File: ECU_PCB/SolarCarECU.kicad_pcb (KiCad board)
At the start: 4 copper layers, 160 x 105.4 mm, 231 parts, among them J2 Screw_Terminal_01x08, J3 Screw_Terminal_01x08, J4 Screw_Terminal_01x08, J5 Screw_Terminal_01x08, J6 Screw_Terminal_01x08, J7 Screw_Terminal_01x08, J8 Screw_Terminal_01x08, Q1 QM6015D, Q2 QM6015D, Q3 QM6015D, Q4 QM6015D, Q5 QM6015D, Q6 QM6015D, Q7 QM6015D, U1 Teensy3.6, U10 LM324A, U11 MCP1403, U2 MCP1403, U3 MCP1403, U4 L7805, U5 MCP2562-E-P, U6 MCP2562-E-P, U7 4504, U8 4504, U9 4504

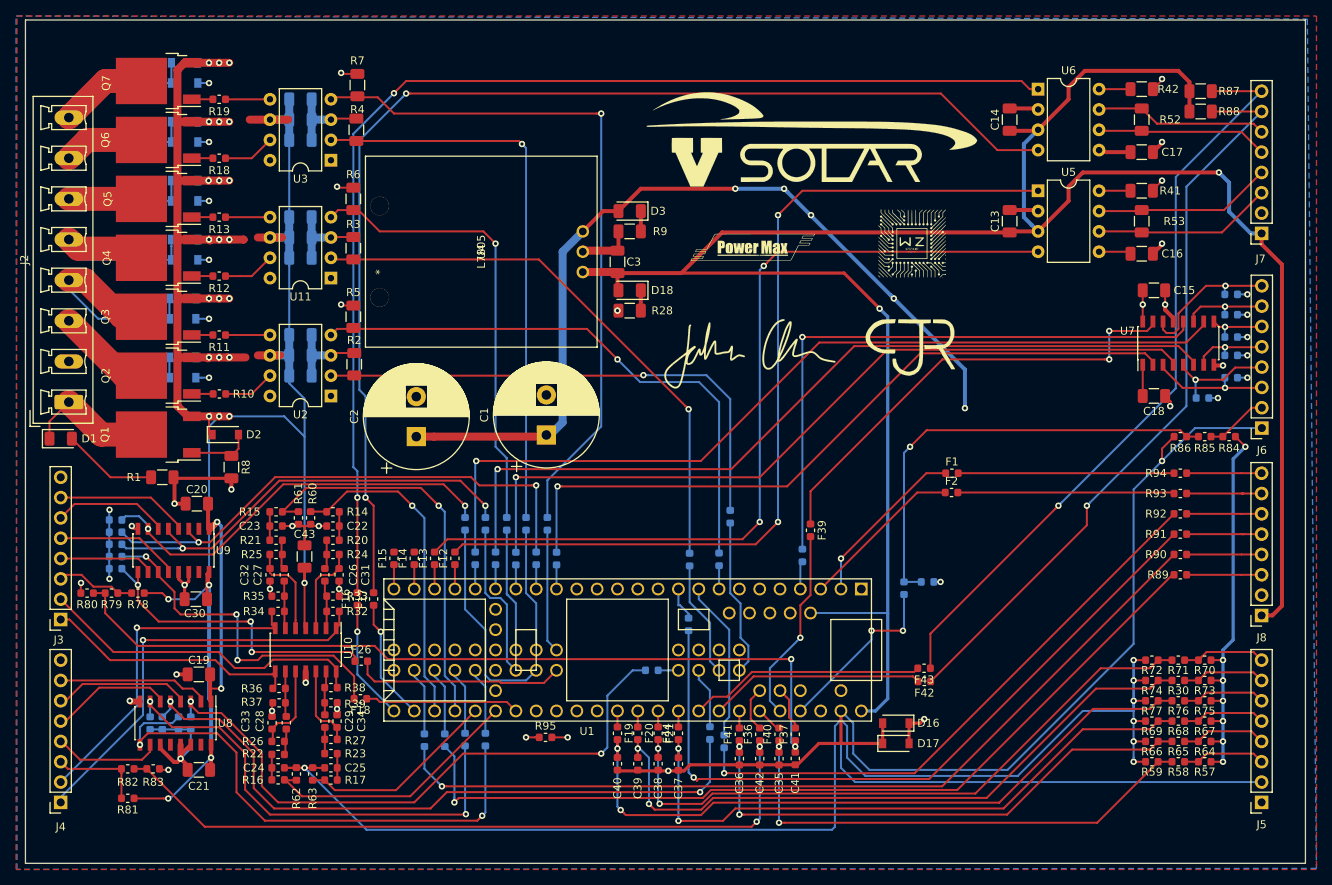
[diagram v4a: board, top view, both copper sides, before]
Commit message: route some traces under 12v plane to reduce resistance per prof. powell
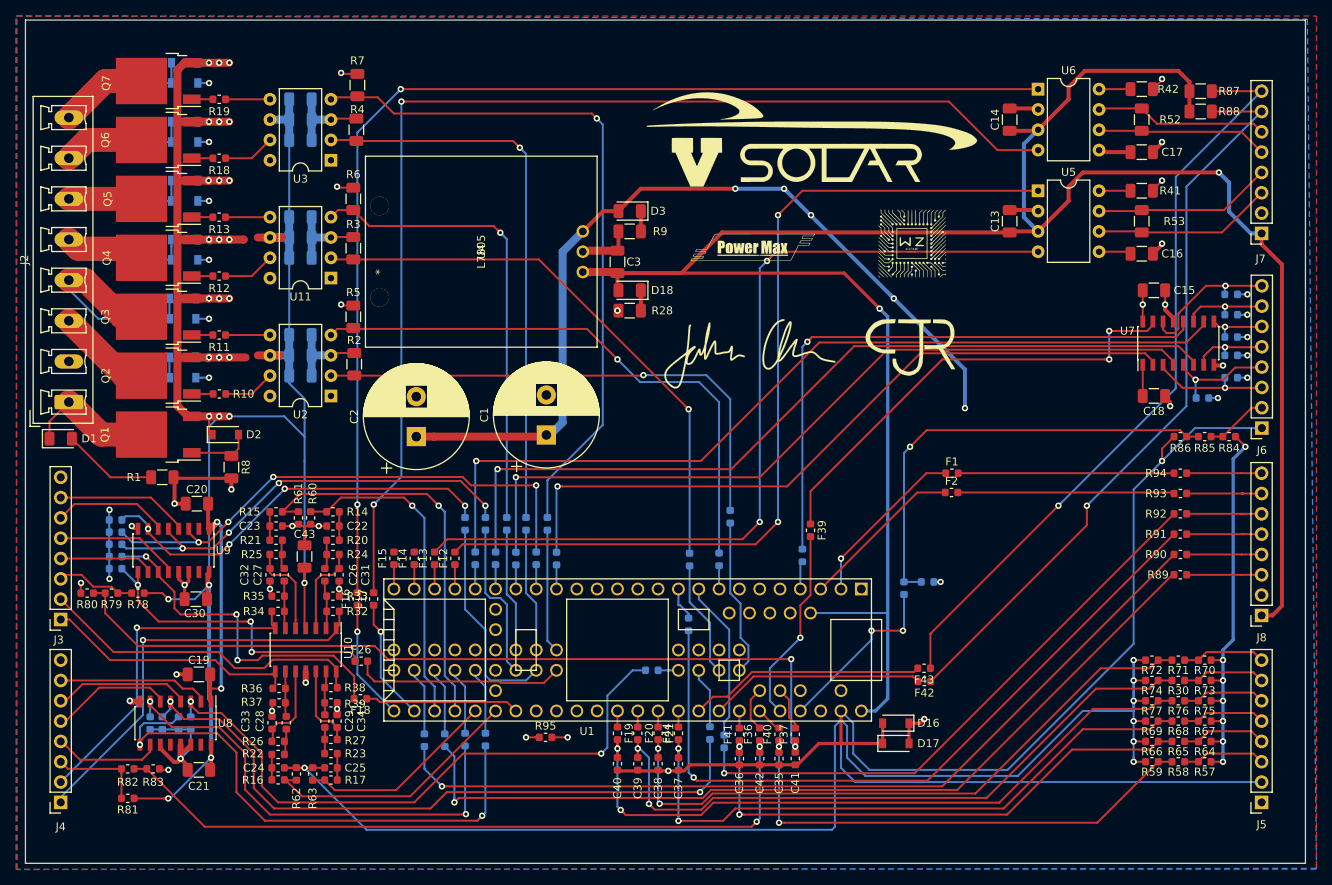
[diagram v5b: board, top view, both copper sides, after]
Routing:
- net +12V: track 440.0 -> 435.2 mm
- net /CAN1_RX: track 147.5 -> 144.9 mm
- net /CAN1_TX: track 146.3 -> 144.9 mm
- net /LV_HEADLIGHTS: track 57.5 -> 58.6 mm
- net /LV_KILL_SENSE: track 75.6 -> 74.8 mm
- net /PWM_MOTOR_L_THROTTLE: track 41.3 -> 40.7 mm
- net /PWM_MOTOR_L_REGEN: track 50.2 -> 49.6 mm
- net /SDA_0: track 96.1 -> 95.5 mm
- net /LV_LEFT_BLINKERS: track 88.0 -> 87.5 mm
- net /LV_MOTOR_R_FWD_EN: track 51.8 -> 51.6 mm, vias 2 -> 4
- net /LV_MOTOR_R_REV_EN: track 55.2 -> 55.3 mm, vias 2 -> 4
- net /LV_HAZARD_LED: track 66.6 -> 66.7 mm, vias 2 -> 4

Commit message: thickened up some traces
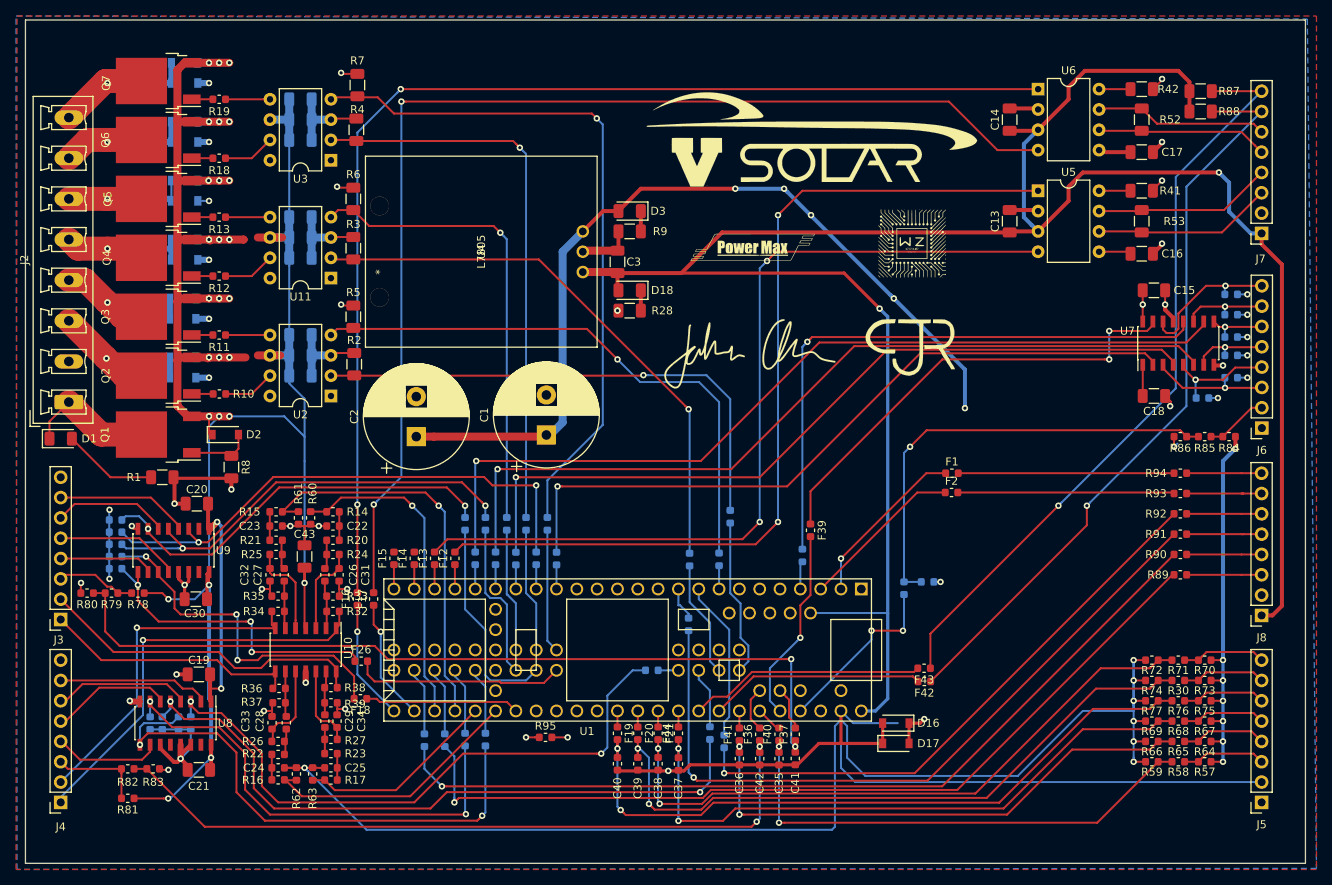
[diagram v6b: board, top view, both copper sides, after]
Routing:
- net GNDA: track 378.7 -> 302.0 mm
- net +12V: track 435.2 -> 458.3 mm
- net /HORN: track 30.7 -> 32.2 mm, vias 0 -> 1
- net /STROBE: track 28.8 -> 30.3 mm, vias 0 -> 1
- net /LV_MOTOR_R_METER: track 105.4 -> 106.7 mm
- net /LEFT_BLINKERS: track 28.8 -> 28.1 mm, vias 0 -> 1
- net /RIGHT_BLINKERS: track 26.9 -> 26.2 mm, vias 0 -> 1
- net /LV_MOTOR_R_REV_EN: track 55.3 -> 55.0 mm, vias 4 -> 2
- net /LV_MOTOR_R_FWD_EN: track 51.6 -> 51.5 mm, vias 4 -> 2
- net /BRAKELIGHTS: track 27.1 -> 27.0 mm, vias 0 -> 1
- net /LV_HAZARD_LED: vias 4 -> 2
- net /HEADLIGHTS: vias 0 -> 1

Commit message: fix 12v islands and added vias that max removed
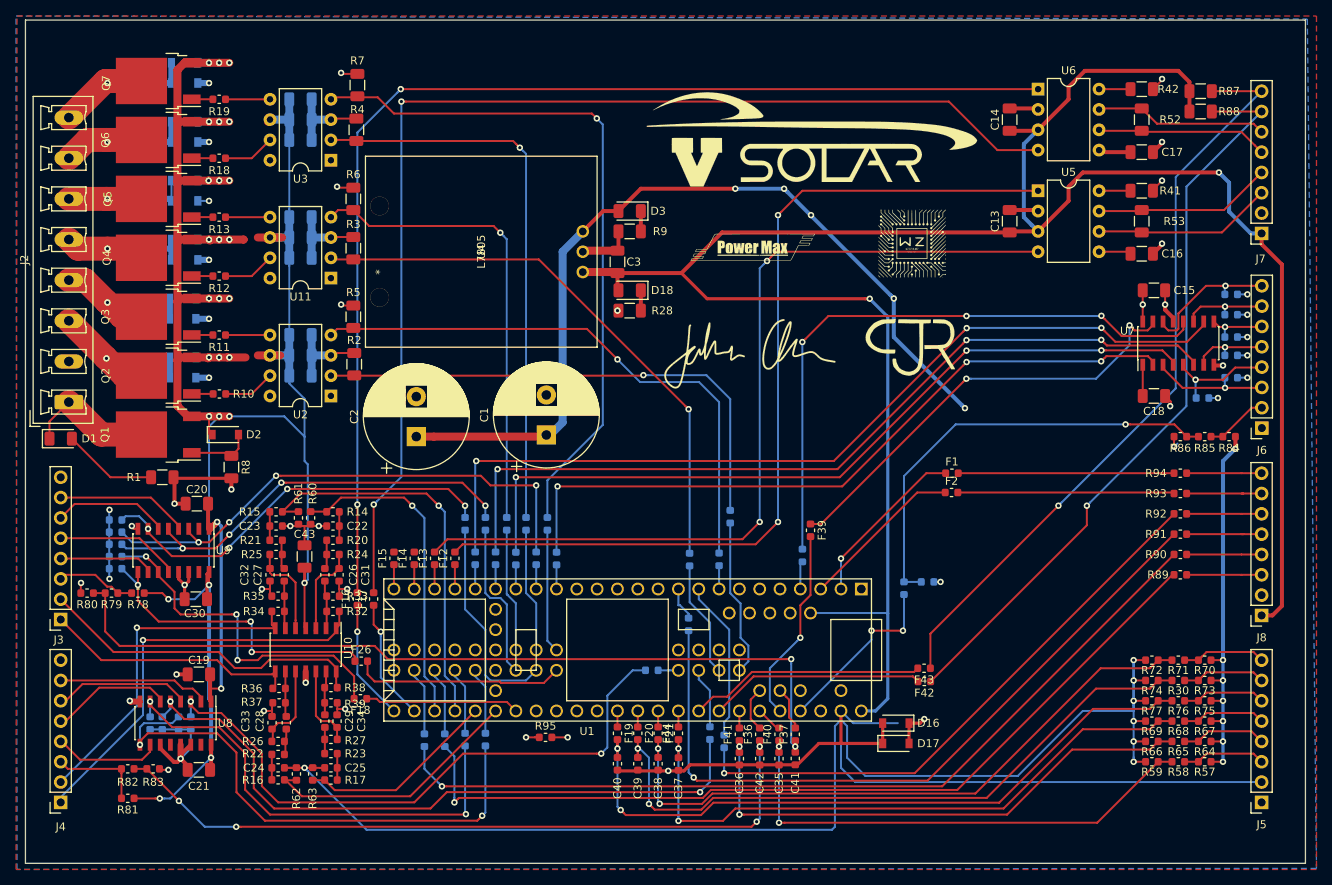
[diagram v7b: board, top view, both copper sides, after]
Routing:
- net /LV_HORN_CTRL: track 58.0 -> 55.5 mm
- net /LV_KILL_SENSE: track 74.8 -> 77.3 mm, vias 1 -> 3
- net /LV_SEL_CTRL: track 109.8 -> 111.3 mm, vias 1 -> 3
- net /LV_HEADLIGHT_CTRL: track 56.6 -> 55.5 mm
- net /LV_UP_CTRL: track 105.1 -> 105.7 mm, vias 1 -> 3
- net /HORN_CTRL: track 18.2 -> 17.6 mm
- net /LV_HAZARD_CTRL: track 90.5 -> 90.2 mm, vias 1 -> 3
- net /LV_HAZARD_LED: track 66.7 -> 66.8 mm, vias 2 -> 4
- net /LV_MOTOR_R_FWD_EN: track 51.5 -> 51.6 mm, vias 2 -> 4
- net /LV_DOWN_CTRL: track 99.2 -> 99.1 mm, vias 1 -> 3
- net /LV_MOTOR_R_REV_EN: vias 2 -> 4
- net /LV_MOTOR_L_METER: vias 2 -> 4

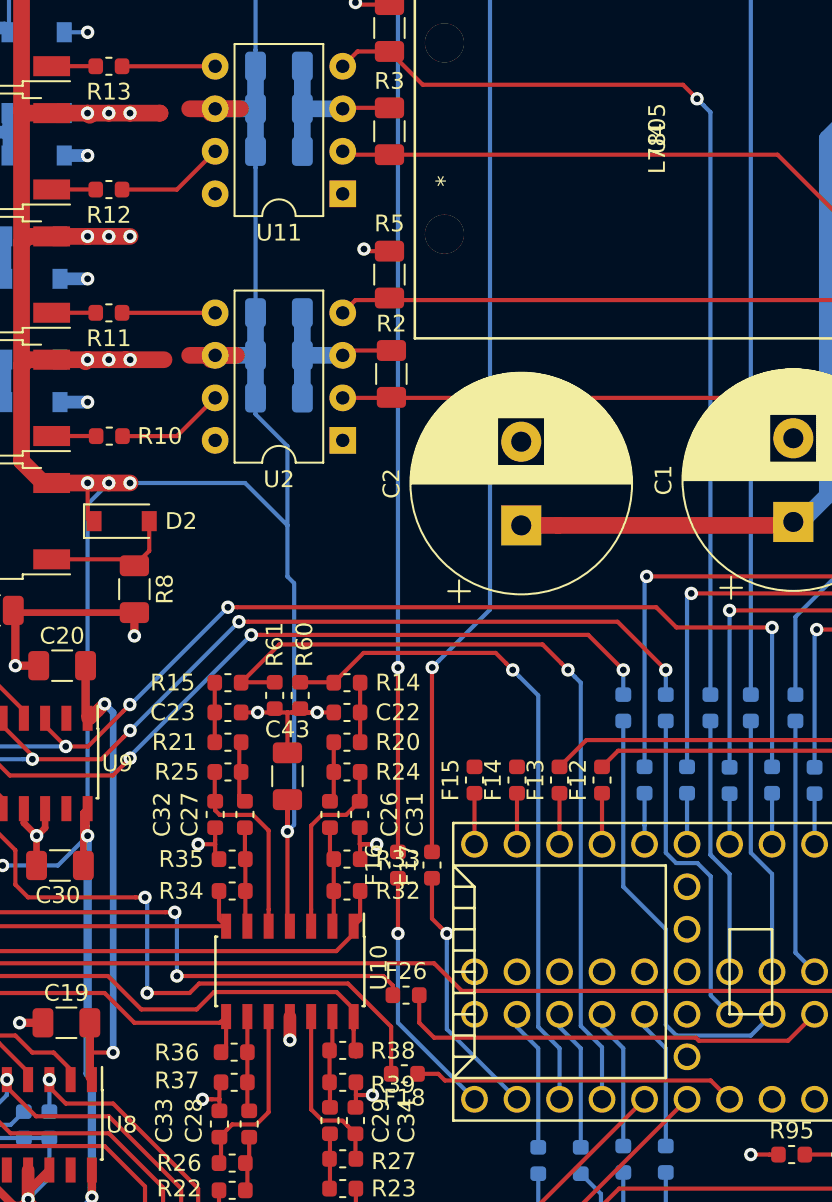
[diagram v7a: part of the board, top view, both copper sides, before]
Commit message: fix weird remnants of 12v traces
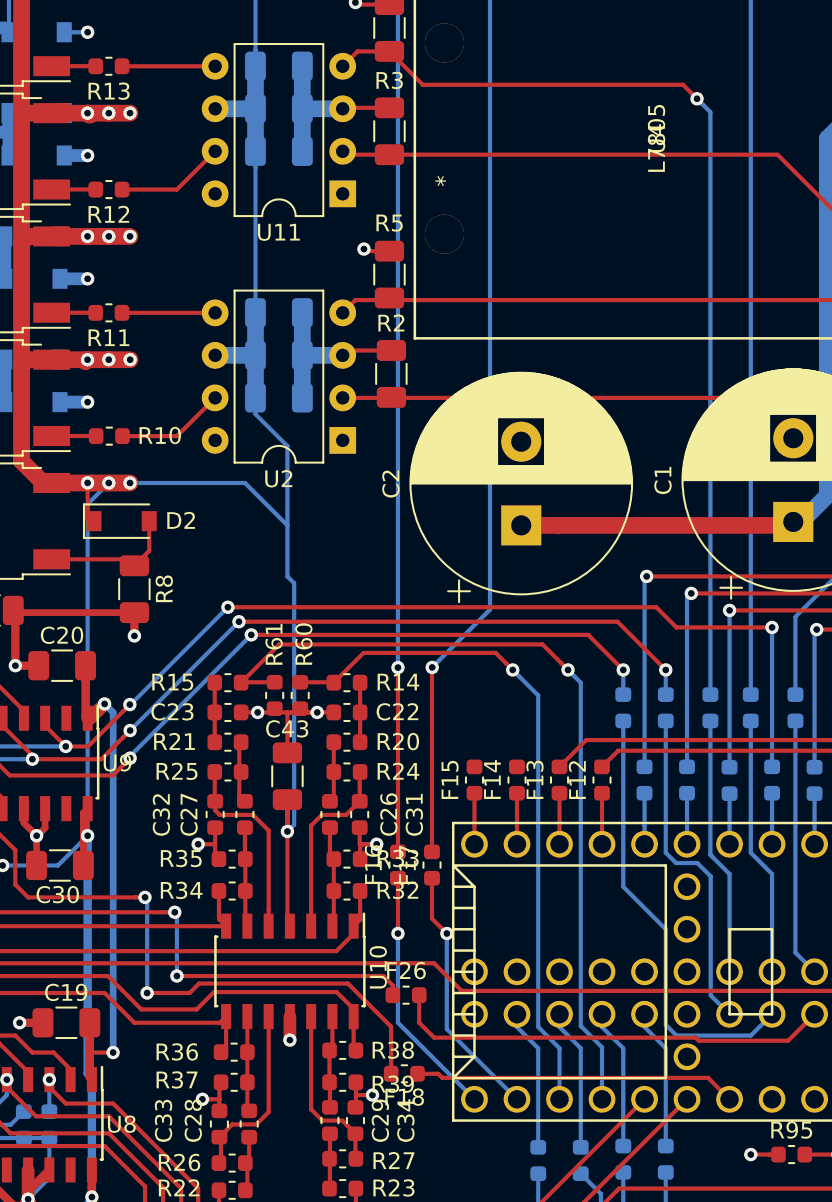
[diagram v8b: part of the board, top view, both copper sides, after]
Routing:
- net +12V: track 458.6 -> 448.3 mm
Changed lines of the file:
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@@
     (thickness 1.6)
     (drawings 6)
-    (tracks 1551)
+    (tracks 1544)
     (zones 0)
     (modules 231)
@@
   (segment (start 98.8 52.584) (end 99.06 52.324) (width 1) (layer F.Cu) (net 1))
   (segment (start 89.29 52.584) (end 91.434 52.584) (width 1) (layer F.Cu) (net 1))
-  (segment (start 98.8 67.316) (end 99.06 67.056) (width 1) (layer F.Cu) (net 1))
   (segment (start 89.29 67.316) (end 91.434 67.316) (width 1) (layer F.Cu) (net 1))
-  (segment (start 98.8 82.048) (end 99.06 81.788) (width 1) (layer F.Cu) (net 1))
   (segment (start 89.29 82.048) (end 91.434 82.048) (width 1) (layer F.Cu) (net 1))
   (segment (start 89.29 89.414) (end 91.688 89.414) (width 1) (layer F.Cu) (net 1))
@@
   (via (at 91.434 82.048) (size 0.8) (drill 0.4) (layers F.Cu B.Cu) (net 1))
   (via (at 93.98 82.048) (size 0.8) (drill 0.4) (layers F.Cu B.Cu) (net 1))
-  (segment (start 92.704 82.048) (end 93.72 82.048) (width 1) (layer F.Cu) (net 1))
   (via (at 92.704 82.048) (size 0.8) (drill 0.4) (layers F.Cu B.Cu) (net 1))
   (segment (start 91.434 67.316) (end 92.704 67.316) (width 1) (layer F.Cu) (net 1))
@@
   (segment (start 91.564 67.446) (end 91.434 67.316) (width 1) (layer F.Cu) (net 1))
   (segment (start 117.348 91.948) (end 119.548 91.948) (width 1) (layer F.Cu) (net 1))
-  (segment (start 95.758 67.31) (end 95.764 67.316) (width 1) (layer F.Cu) (net 1))
-  (segment (start 93.974 67.316) (end 95.764 67.316) (width 1) (layer F.Cu) (net 1))
-  (segment (start 97.536 67.056) (end 100.572 67.056) (width 1) (layer F.Cu) (net 1))
-  (segment (start 93.72 82.048) (end 96.006 82.048) (width 1) (layer F.Cu) (net 1))
-  (segment (start 97.536 81.788) (end 100.33 81.788) (width 1) (layer F.Cu) (net 1))
   (segment (start 101.47 49.784) (end 101.47 54.864) (width 1) (layer B.Cu) (net 1))
   (segment (start 99.06 52.324) (end 101.47 52.324) (width 1) (layer B.Cu) (net 1))
@@
   (segment (start 82.0675 137.033) (end 82.211911 137.177411) (width 0.25) (layer F.Cu) (net 1))
   (segment (start 85.846552 137.177411) (end 85.280867 137.177411) (width 0.25) (layer B.Cu) (net 1))
+  (segment (start 92.704 82.048) (end 93.98 82.048) (width 1) (layer F.Cu) (net 1))
   (via (at 210.566 67.818) (size 0.8) (drill 0.4) (layers F.Cu B.Cu) (net 2))
   (via (at 142.494 76.2) (size 0.8) (drill 0.4) (layers F.Cu B.Cu) (net 2))
@@
   (segment (start 117.094 126.238) (end 112.903004 122.047004) (width 0.25) (layer B.Cu) (net 174))
   (segment (start 112.014 115.442996) (end 112.503005 115.932001) (width 0.25) (layer F.Cu) (net 174))
-  (segment (start 128.668999 125.112999) (end 112.786983 125.112999) (width 0.25) (layer F.Cu) (net 175))
-  (segment (start 129.794 126.238) (end 128.668999 125.112999) (width 0.25) (layer F.Cu) (net 175))
   (segment (start 112.387984 124.714) (end 111.1505 124.714) (width 0.25) (layer F.Cu) (net 175))
-  (segment (start 112.786983 125.112999) (end 112.387984 124.714) (width 0.25) (layer F.Cu) (net 175))
+  (segment (start 112.631824 124.95784) (end 112.387984 124.714) (width 0.25) (layer F.Cu) (net 175))
+  (segment (start 129.794 126.238) (end 128.51384 124.95784) (width 0.25) (layer F.Cu) (net 175))
+  (segment (start 128.51384 124.95784) (end 112.631824 124.95784) (width 0.25) (layer F.Cu) (net 175))
   (segment (start 142.494 128.3715) (end 142.494 126.238) (width 0.25) (layer F.Cu) (net 176))
   (segment (start 145.034 126.238) (end 145.034 128.3715) (width 0.25) (layer F.Cu) (net 177))
